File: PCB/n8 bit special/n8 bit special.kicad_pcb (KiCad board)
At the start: 4 copper layers, 99.9 x 100 mm, 47 parts, among them J1 USB_B_Micro, J2 PORT0, J3 PORT1, J4 PORT2, J6 Conn_02x08_Odd_Even, Q1 2N3904, SW1 SW_Push_Dual, U1 W65C02SxP, U10 74HC00, U2 CY62256-70PC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

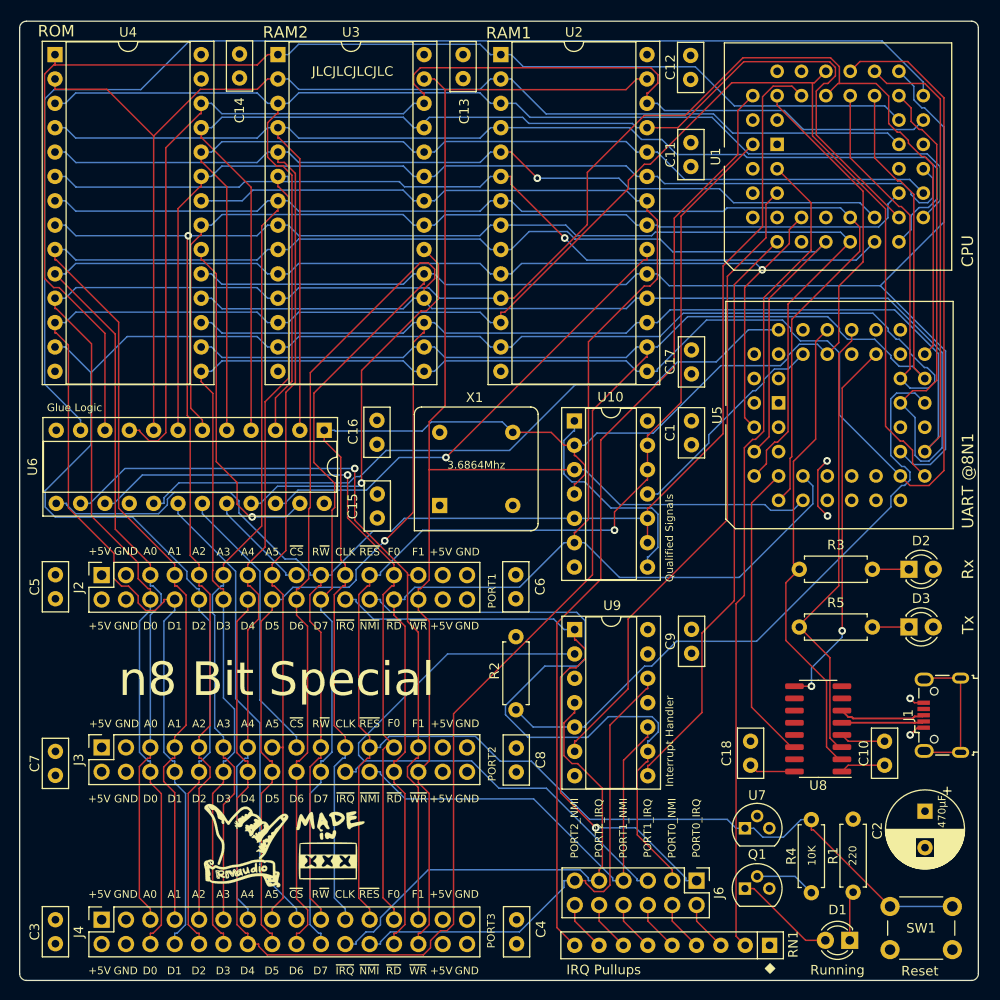
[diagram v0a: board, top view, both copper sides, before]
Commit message: Pre-import stage of autorouting
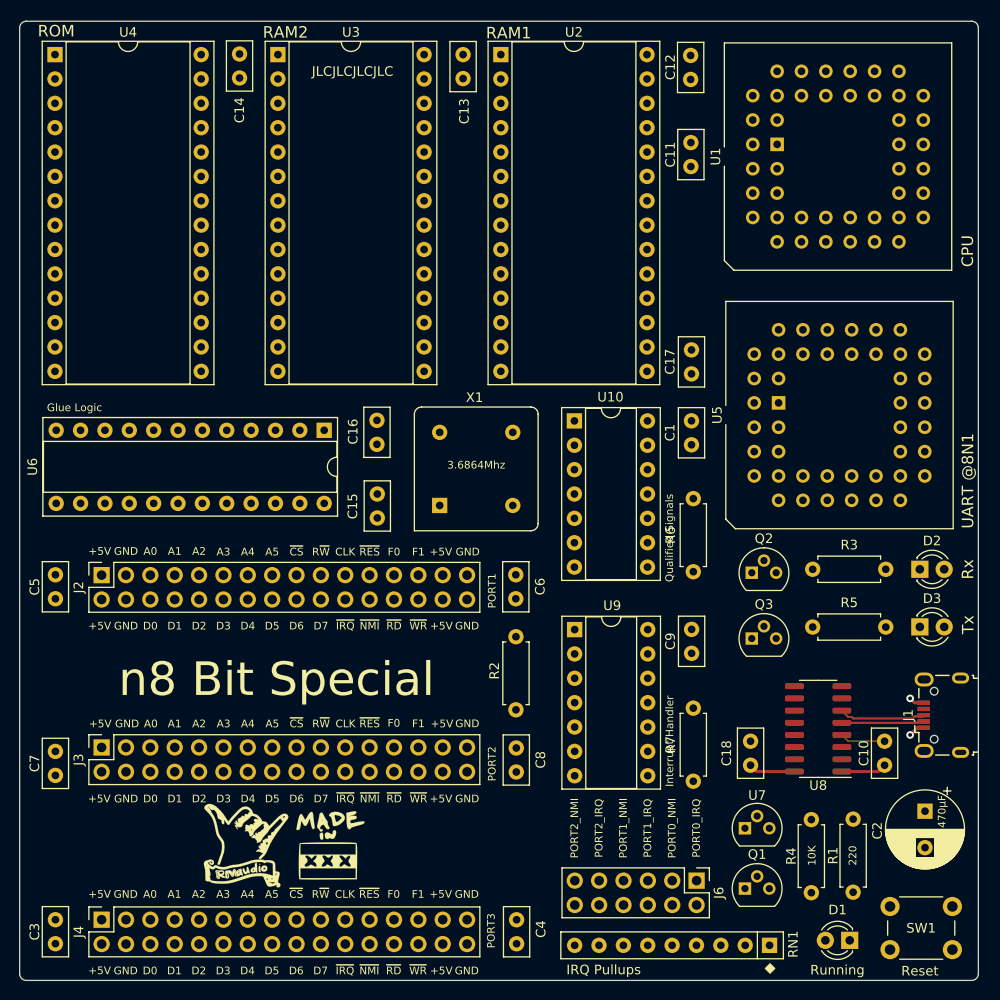
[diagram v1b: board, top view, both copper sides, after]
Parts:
- added Q2: 2N3906, Package_TO_SOT_THT:TO-92, F.Cu at (163.3, 97.4)
- added Q3: 2N3906, Package_TO_SOT_THT:TO-92, F.Cu at (163.3, 104.2)
- added R6: 1K, Resistor_THT:R_Axial_DIN0207_L6.3mm_D2.5mm_P7.62mm_Horizontal, F.Cu at (157.2, 97.3)
- added R7: 1K, Resistor_THT:R_Axial_DIN0207_L6.3mm_D2.5mm_P7.62mm_Horizontal, F.Cu at (157.2, 119.1)
- moved R3 1.40 mm to (177.3, 97.0)
- moved R5 1.40 mm to (177.3, 103.0)
- moved D2 1.14 mm to (180.8, 97.0)
- moved D3 1.14 mm to (180.8, 103.0)
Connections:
- D2 pad 2: +5V -> Net-(D2-Pad2)
- D3 pad 2: +5V -> Net-(D3-Pad2)
- R3 pad 2: RxD -> GND
- R5 pad 2: TxD -> GND
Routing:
- net /D4: track 243.9 -> 0.00 mm
- net /D6: track 221.7 -> 0.00 mm
- net /D1: track 216.3 -> 0.00 mm
- net /D5: track 215.1 -> 0.00 mm, vias 1 -> 0
- net /D2: track 213.0 -> 0.00 mm
- net /D0: track 210.3 -> 0.00 mm
- net /D3: track 207.0 -> 0.00 mm
- net /D7: track 204.5 -> 0.00 mm
- net /A3: track 198.7 -> 0.00 mm
- net /A2: track 188.5 -> 0.00 mm, vias 1 -> 0
- net /A1: track 186.5 -> 0.00 mm
- net ~{RES}: track 182.9 -> 0.00 mm, vias 1 -> 0
- net ~{READ}: track 180.8 -> 0.00 mm
- net /A4: track 175.3 -> 0.00 mm, vias 1 -> 0
- net /A0: track 174.7 -> 0.00 mm, vias 1 -> 0
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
